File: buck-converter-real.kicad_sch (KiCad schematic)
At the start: 56 parts, among them J1 Conn_01x02_Pin, J2 XT60, J3 Battery out (3V6-4V2) NiMH 3S, J4 Conn_01x02, J6 DM3CS-SF, Q1 Q_NMOS_DGS, Q2 CSD18540Q5B - 60-V, Q3 Q_PMOS_DGS, U1 AP2112K-3.3 (3V3 LDO), U5 LM5109BMA (Mosfet Driver), U6 AS78L12RTR-G1 (12V LDO)

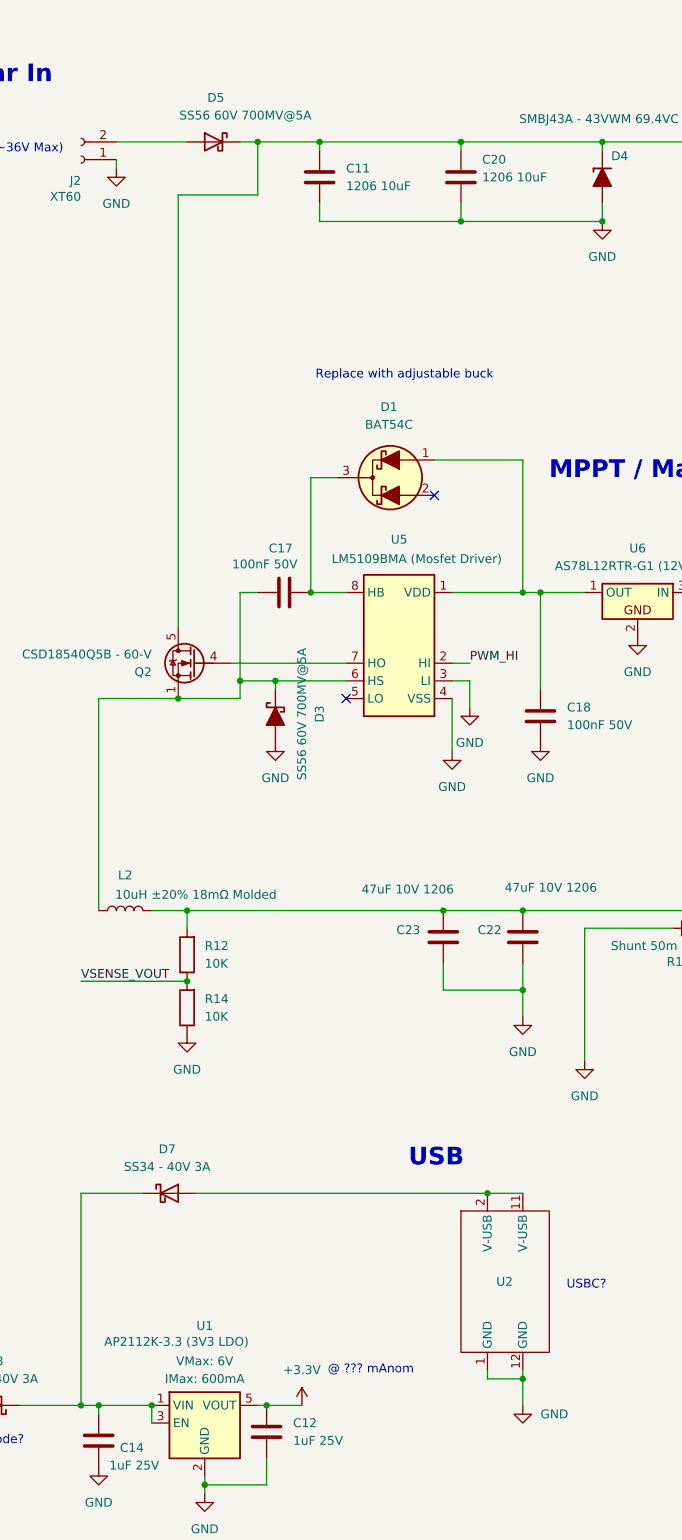
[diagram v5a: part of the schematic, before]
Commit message: Update PCB routing
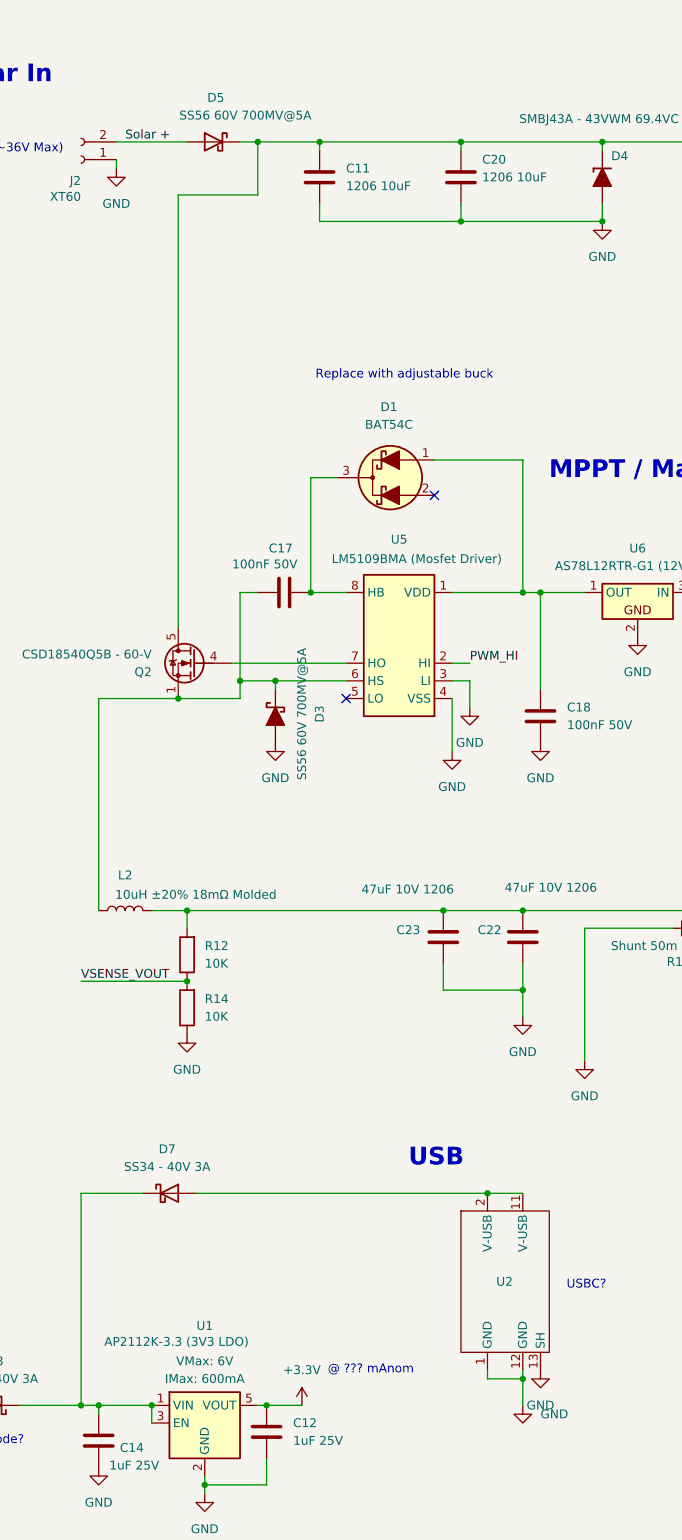
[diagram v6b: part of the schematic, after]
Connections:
- net GND: now also U2.13 (SH)
- net Solar +: now reaches D5.2 (A), J2.2 (Pin_2)
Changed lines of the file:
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@@
 		)
 	)
+	(label "Solar +"
+		(at 73.66 64.77 0)
+		(effects
+			(font
+				(size 1.27 1.27)
+			)
+			(justify left bottom)
+		)
+	)
 	(label "SPI-CITO"
 		(at 306.07 107.95 0)
@@
 		(pin "2"
 		)
+		(pin "13"
+		)
 		(instances
 			(project "buck-converter-real"
@@
 					(unit 1)
 				)
+			)
+		)
+	)
+	(symbol
+		(lib_id "power:GND")
+		(at 133.35 241.3 0)
+		(unit 1)
+		(body_style 1)
+		(exclude_from_sim no)
+		(in_bom yes)
+		(on_board yes)
+		(in_pos_files yes)
+		(dnp no)
+		(fields_autoplaced yes)
+		(property "Reference" "#PWR047"
+			(at 133.35 247.65 0)
+			(hide yes)
+			(show_name no)
+			(do_not_autoplace no)
+			(effects
+				(font
+					(size 1.27 1.27)
+				)
+			)
+		)
+		(property "Value" "GND"
+			(at 133.35 246.38 0)
+			(show_name no)
+			(do_not_autoplace no)
+			(effects
+				(font
+					(size 1.27 1.27)
+				)
+			)
+		)
+		(property "Footprint" ""
+			(at 133.35 241.3 0)
+			(hide yes)
+			(show_name no)
+			(do_not_autoplace no)
+			(effects
+				(font
+					(size 1.27 1.27)
+				)
+			)
+		)
+		(property "Datasheet" ""
+			(at 133.35 241.3 0)
+			(hide yes)
+			(show_name no)
+			(do_not_autoplace no)
+			(effects
+				(font
+					(size 1.27 1.27)
+				)
+			)
+		)
+		(property "Description" "Power symbol creates a global label with name \"GND\" , ground"
+			(at 133.35 241.3 0)
+			(hide yes)
+			(show_name no)
+			(do_not_autoplace no)
+			(effects
+				(font
+					(size 1.27 1.27)
+				)
+			)
+		)
+		(pin "1"
+		)
+		(instances
+			(project "buck-converter-real"
+				(path "/cbc98a1b-0533-4e8d-81af-0515d3e50555"
+					(reference "#PWR047")
+					(unit 1)
+				)

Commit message: Update PCB routing
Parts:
- removed BOOT1: Boot, Connector_PinSocket_2.54mm:PinSocket_1x03_P2.54mm_Vertical, symbol Connector:Conn_01x03_Pin
- removed GPIO1, J1: Conn_01x02_Pin, Connector_PinHeader_2.54mm:PinHeader_1x02_P2.54mm_Vertical, symbol Connector:Conn_01x02_Pin
- removed I2C1: I2C1, Connector_PinSocket_2.54mm:PinSocket_1x04_P2.54mm_Vertical, symbol Connector:Conn_01x04_Pin
- removed SWD1: SWD, Connector_PinSocket_2.54mm:PinSocket_1x04_P2.54mm_Vertical, symbol Connector:Conn_01x04_Pin
- removed UART1, UART2: UART, Connector_PinSocket_2.54mm:PinSocket_1x03_P2.54mm_Vertical, symbol Connector:Conn_01x03_Pin
- added GPIO1: GPIO, symbol Connector_Generic:Conn_01x02
- added J1: BOOT, Connector_PinHeader_2.54mm:PinHeader_1x03_P2.54mm_Vertical, symbol Connector_Generic:Conn_01x03
- added J5: UART 2, Connector_PinHeader_2.54mm:PinHeader_1x03_P2.54mm_Vertical, symbol Connector_Generic:Conn_01x03
- added J7: UART 1, Connector_PinHeader_2.54mm:PinHeader_1x03_P2.54mm_Vertical, symbol Connector_Generic:Conn_01x03
- added J8: I2C, Connector_PinHeader_2.54mm:PinHeader_1x04_P2.54mm_Vertical, symbol Connector_Generic:Conn_01x04
- added J9: SWD, Connector_PinHeader_2.54mm:PinHeader_1x04_P2.54mm_Vertical, symbol Connector_Generic:Conn_01x04
- J4: value Conn_01x02 -> POWER
- renumbered U2 to USBC
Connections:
- net +3.3V: now also C10.1, C9.1, J4.1 (Pin_1), J1.1 (Pin_1), J8.3 (Pin_3), J9.1 (Pin_1); no longer C10.2, C9.2
- net BOOT: now also J1.2 (Pin_2)
- net GND: now also C10.2, C9.2, J4.2 (Pin_2), GPIO1.2 (Pin_2), J1.3 (Pin_3), J5.1 (Pin_1), J7.1 (Pin_1), J8.4 (Pin_4), J9.4 (Pin_4); no longer C10.1, C9.1
- net GPIO-10: now also GPIO1.1 (Pin_1)
- net I2C-SCL: now also J8.1 (Pin_1)
- net I2C-SDA: now also J8.2 (Pin_2)
- net SWCLK: now also J9.3 (Pin_3)
- net SWDIO: now also J9.2 (Pin_2)
- net UART-1-RX: now also J7.3 (Pin_3)
- net UART-1-TX: now also J7.2 (Pin_2)
- net UART-2-RX: now also J5.2 (Pin_2)
- net UART-2-TX: now also J5.3 (Pin_3)
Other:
- note added: "POWER"
- note added: "Replace with adjustable buck?"
- note added: "WIO-E5 MCU"
- note removed: "Headers"
- note removed: "LEDs"
- note removed: "Replace with adjustable buck"
- note removed: "USB"
- note removed: "WIO-E5 MCU/LORA"
- moved on the sheet: C10, C11, C12, C13, C14, C15, C17, C18, C19, C20, C22, C23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
